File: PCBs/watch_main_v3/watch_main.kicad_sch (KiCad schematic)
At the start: 1 part, among them U101 Watch_Outline_V2

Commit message: watch_main_v3 updates
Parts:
- U101: footprint watch_footprints:Watch Outline V2 -> watch_footprints:Watch Outline V3; symbol watch_symbols_lib:Watch_Outline_V2 -> watch_symbols_lib:Watch_Outline_V3
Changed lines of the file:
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@@
     )
   )
-  (symbol (lib_id "watch_symbols_lib:Watch_Outline_V2") (at 73.66 177.8 0) (unit 1)
+  (symbol (lib_id "watch_symbols_lib:Watch_Outline_V3") (at 73.66 177.8 0) (unit 1)
     (in_bom no) (on_board yes) (dnp no) (fields_autoplaced)
-    (property "Reference" "U101" (at 82.55 177.165 0)
+    (property "Reference" "U101" (at 82.55 176.53 0)
       (effects (font (size 1.27 1.27)) (justify left))
     )
-    (property "Value" "Watch_Outline_V2" (at 82.55 179.705 0)
+    (property "Value" "Watch_Outline_V2" (at 82.55 179.07 0)
       (effects (font (size 1.27 1.27)) (justify left))
     )
-    (property "Footprint" "watch_footprints:Watch Outline V2" (at 73.66 187.96 0)
+    (property "Footprint" "watch_footprints:Watch Outline V3" (at 73.66 187.96 0)
       (effects (font (size 1.27 1.27)) hide)
     )

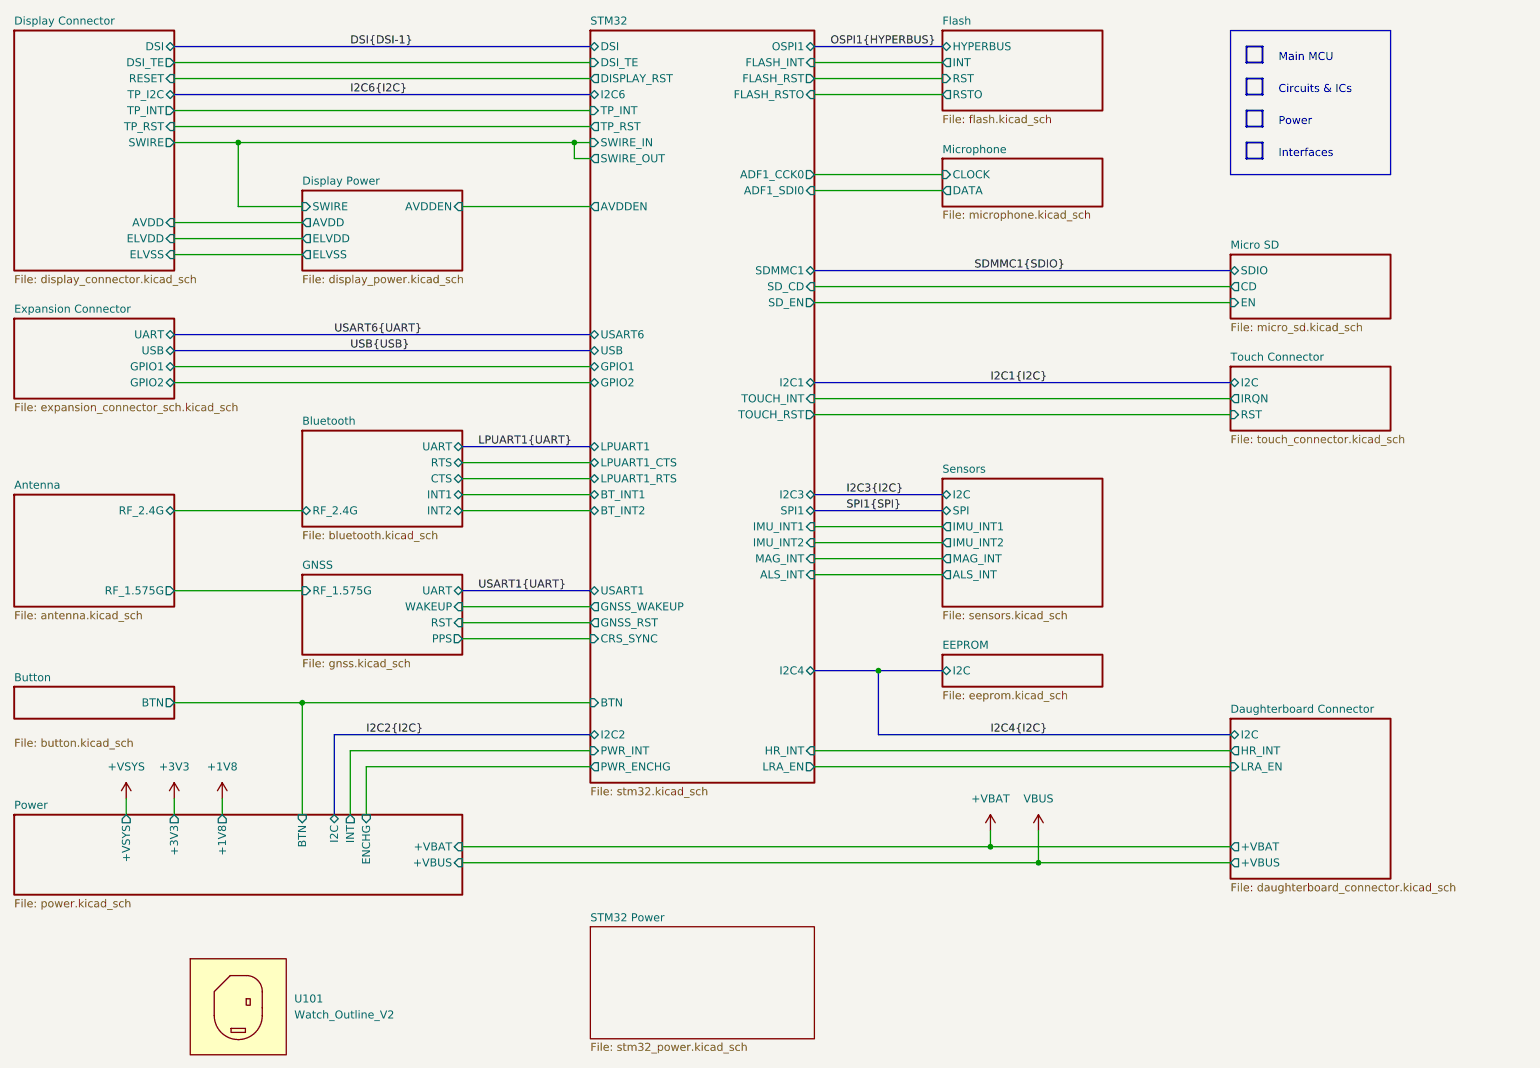
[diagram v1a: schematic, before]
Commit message: watch_main_v3 WiFi/Bluetooth schematic done
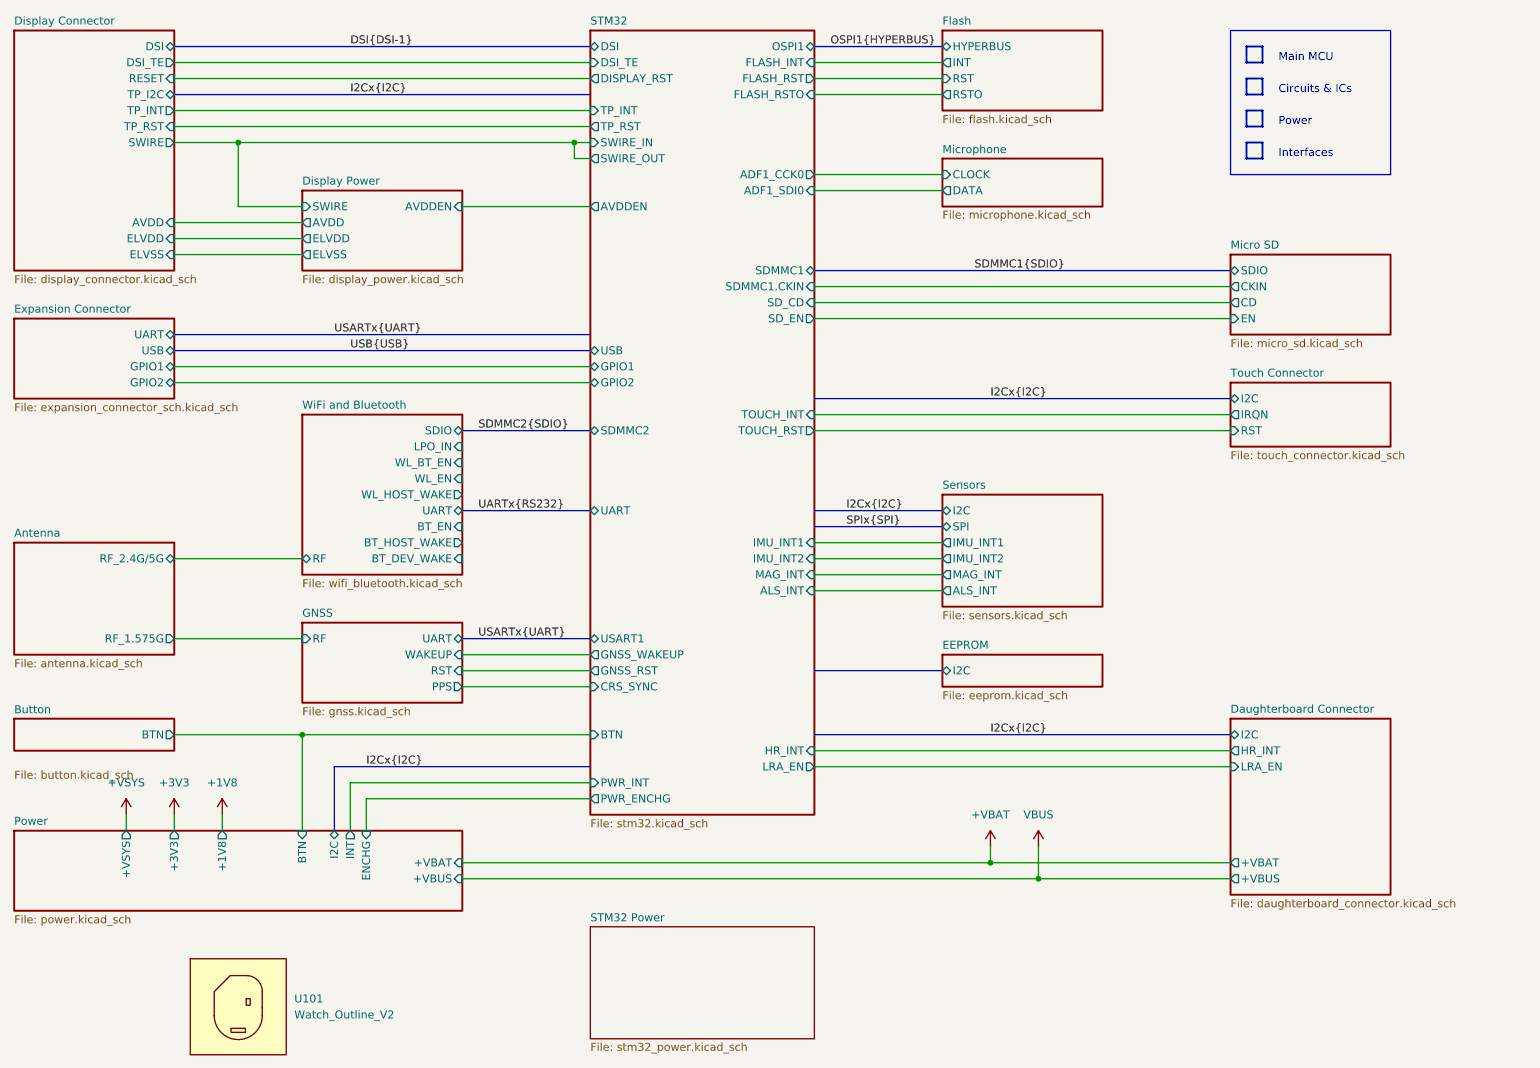
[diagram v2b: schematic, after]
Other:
- sheet Bluetooth renamed WiFi and Bluetooth
- sheet Antenna ports: added RF_2.4G/5G; removed RF_2.4G
- sheet GNSS ports: added RF; removed RF_1.575G
- sheet Micro SD ports: added CKIN; removed none
- sheet STM32 ports: added SDMMC1.CKIN, SDMMC2, UART; removed BT_INT1, BT_INT2, I2C1, I2C2, I2C3, I2C4, I2C6, LPUART1, LPUART1_CTS, LPUART1_RTS, SPI1, USART6
- sheet WiFi and Bluetooth: file bluetooth.kicad_sch -> wifi_bluetooth.kicad_sch
- sheet WiFi and Bluetooth ports: added BT_DEV_WAKE, BT_EN, BT_HOST_WAKE, LPO_IN, RF, SDIO, WL_BT_EN, WL_EN, WL_HOST_WAKE; removed CTS, INT1, INT2, RF_2.4G, RTS

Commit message: PCB V3 progress
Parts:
- added R101: 0R, Resistor_SMD:R_0402_1005Metric, symbol Device:R_Small
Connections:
- new net SWIRE_IN: R101.1
- new net SWIRE_OUT: R101.2
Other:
- sheet Daughterboard Connector ports: added VBUS_ADC; removed none
- sheet Display Power ports: added AVDD_ADC, ELVDD_ADC, ELVSS_ADC; removed none
- sheet STM32 ports: added AVDD_ADC, BT_DEV_WAKE, BT_EN, BT_HOST_WAKE, ELVDD_ADC, ELVSS_ADC, GNSS_PPS, I2C1, I2C2, I2C3, I2C4, I2C5, I2C6, RCC_LSCO, SPI1, UART4, USART2, VBUS_ADC, WL_BT_PWR_EN, WL_EN, WL_HOST_WAKE; removed CRS_SYNC, UART
- sheet WiFi and Bluetooth ports: added WL_BT_PWR_EN; removed WL_BT_EN

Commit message: PCB V3 Progress
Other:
- sheet Daughterboard Connector ports: added none; removed VBUS_ADC
- sheet Power ports: added ISYS; removed none
- sheet STM32 ports: added ISYS; removed VBUS_ADC
- note added: "CHANGE VBUS ADC TO VSYS CURRENT SENSE (MAX9938, KDV04DR050ET)"
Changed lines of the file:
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@@
 	(wire
 		(pts
+			(xy 96.52 149.86) (xy 96.52 147.32)
+		)
+		(stroke
+			(width 0)
+			(type default)
+		)
+	)
+	(wire
+		(pts
 			(xy 200.66 157.48) (xy 109.22 157.48)
 		)
@@
 	(wire
 		(pts
+			(xy 96.52 147.32) (xy 129.54 147.32)
+		)
+		(stroke
+			(width 0)
+			(type default)
+		)
+	)
+	(wire
+		(pts
 			(xy 109.22 96.52) (xy 129.54 96.52)
 		)
@@
 	(wire
 		(pts
-			(xy 165.1 142.24) (xy 231.14 142.24)
-		)
-		(stroke
-			(width 0)
-			(type default)
-		)
-	)
-	(wire
-		(pts
 			(xy 165.1 104.14) (xy 185.42 104.14)
 		)
@@
 		)
 	)
+	(text "CHANGE VBUS ADC TO VSYS CURRENT SENSE\n(MAX9938, KDV04DR050ET)"
+		(exclude_from_sim no)
+		(at 180.34 172.72 0)
+		(effects
+			(font
+				(size 2.54 2.54)
+			)
+			(justify left)
+		)
+	)
 	(text "Circuits & ICs"
 		(exclude_from_sim no)
@@
 		)
 	)
-	(label "VBUS_ADC"
-		(at 193.04 142.24 0)
+	(label "ISYS"
+		(at 106.68 147.32 0)
 		(fields_autoplaced yes)
 		(effects
@@
 	(sheet
 		(at 129.54 22.86)
-		(size 35.56 124.46)
+		(size 35.56 127)
 		(fields_autoplaced yes)
 		(stroke
@@
 		)
 		(property "Sheetfile" "stm32.kicad_sch"
-			(at 129.54 147.9808 0)
+			(at 129.54 150.5208 0)
 			(effects
 				(font
@@
 			)
 		)
-		(pin "VBUS_ADC" input
-			(at 165.1 142.24 0)
-			(effects
-				(font
-					(size 1.27 1.27)
-				)
-				(justify right)
-			)
-		)
 		(pin "AVDD_ADC" input
 			(at 129.54 55.88 180)
@@
 			)
 		)
+		(pin "ISYS" input
+			(at 129.54 147.32 180)
+			(effects
+				(font
+					(size 1.27 1.27)
+				)
+				(justify left)
+			)
+		)
 		(instances
 			(project "watch_main"
@@
 			)
 		)
+		(pin "ISYS" output
+			(at 96.52 149.86 90)
+			(effects
+				(font
+					(size 1.27 1.27)
+				)
+				(justify right)
+			)
+		)
 		(instances
 			(project "watch_main"
@@
 			(effects
 				(font
-					(size 1.27 1.27)
-				)
-				(justify left)
-			)
-		)
-		(pin "VBUS_ADC" output
-			(at 231.14 142.24 180)
-			(effects
-				(font

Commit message: Hard routing done
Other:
- note added: "ADD LEDs"
- note removed: "CHANGE VBUS ADC TO VSYS CURRENT SENSE (MAX9938, KDV04DR050ET)"
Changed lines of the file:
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@@
 		)
 	)
-	(text "CHANGE VBUS ADC TO VSYS CURRENT SENSE\n(MAX9938, KDV04DR050ET)"
+	(text "ADD LEDs"
 		(exclude_from_sim no)
 		(at 180.34 172.72 0)

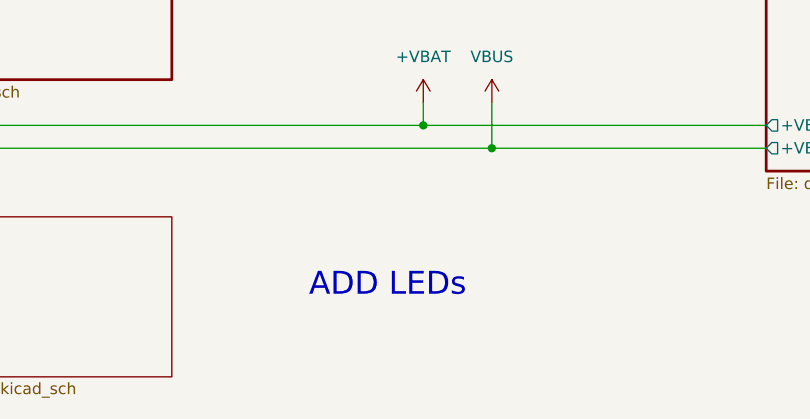
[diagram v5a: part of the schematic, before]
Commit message: Main board version 3.0 done and purchased
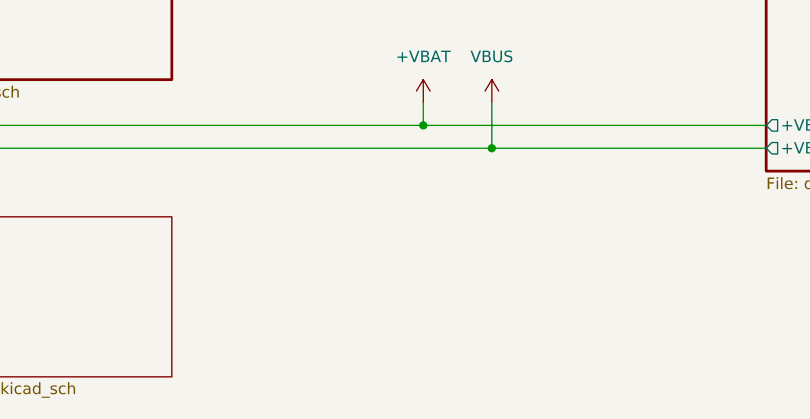
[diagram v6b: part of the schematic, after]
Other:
- note removed: "ADD LEDs"
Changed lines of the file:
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@@
-		)
-	)
-	(text "ADD LEDs"
-		(exclude_from_sim no)
-		(at 180.34 172.72 0)
-		(effects
-			(font
-				(size 2.54 2.54)
-			)
-			(justify left)
 		)
 	)
